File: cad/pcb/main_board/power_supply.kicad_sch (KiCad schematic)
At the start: 7 parts

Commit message: VDDA, BOOT SEL
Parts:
- removed C7: 100nF, symbol Device:C
- removed C8: 1uF, symbol Device:C
- added C10: 1uF, symbol Device:C
- added C11: 100nF, symbol Device:C
- added L1: L, symbol Device:L
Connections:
- net VSSA: now also C10.2, C11.2
- net VBAT renamed +3V3
- net +3V3: now also L1.1
- net VSS renamed GND
- new net VDDA: C10.1, C11.1, L1.2

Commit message: Thermo Couple Pins
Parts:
- C2: value 100nF -> 4u7F
- C6: value 4u7F -> 100nF
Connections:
- net VSSA is gone; now on net GND: C10.2, C11.2

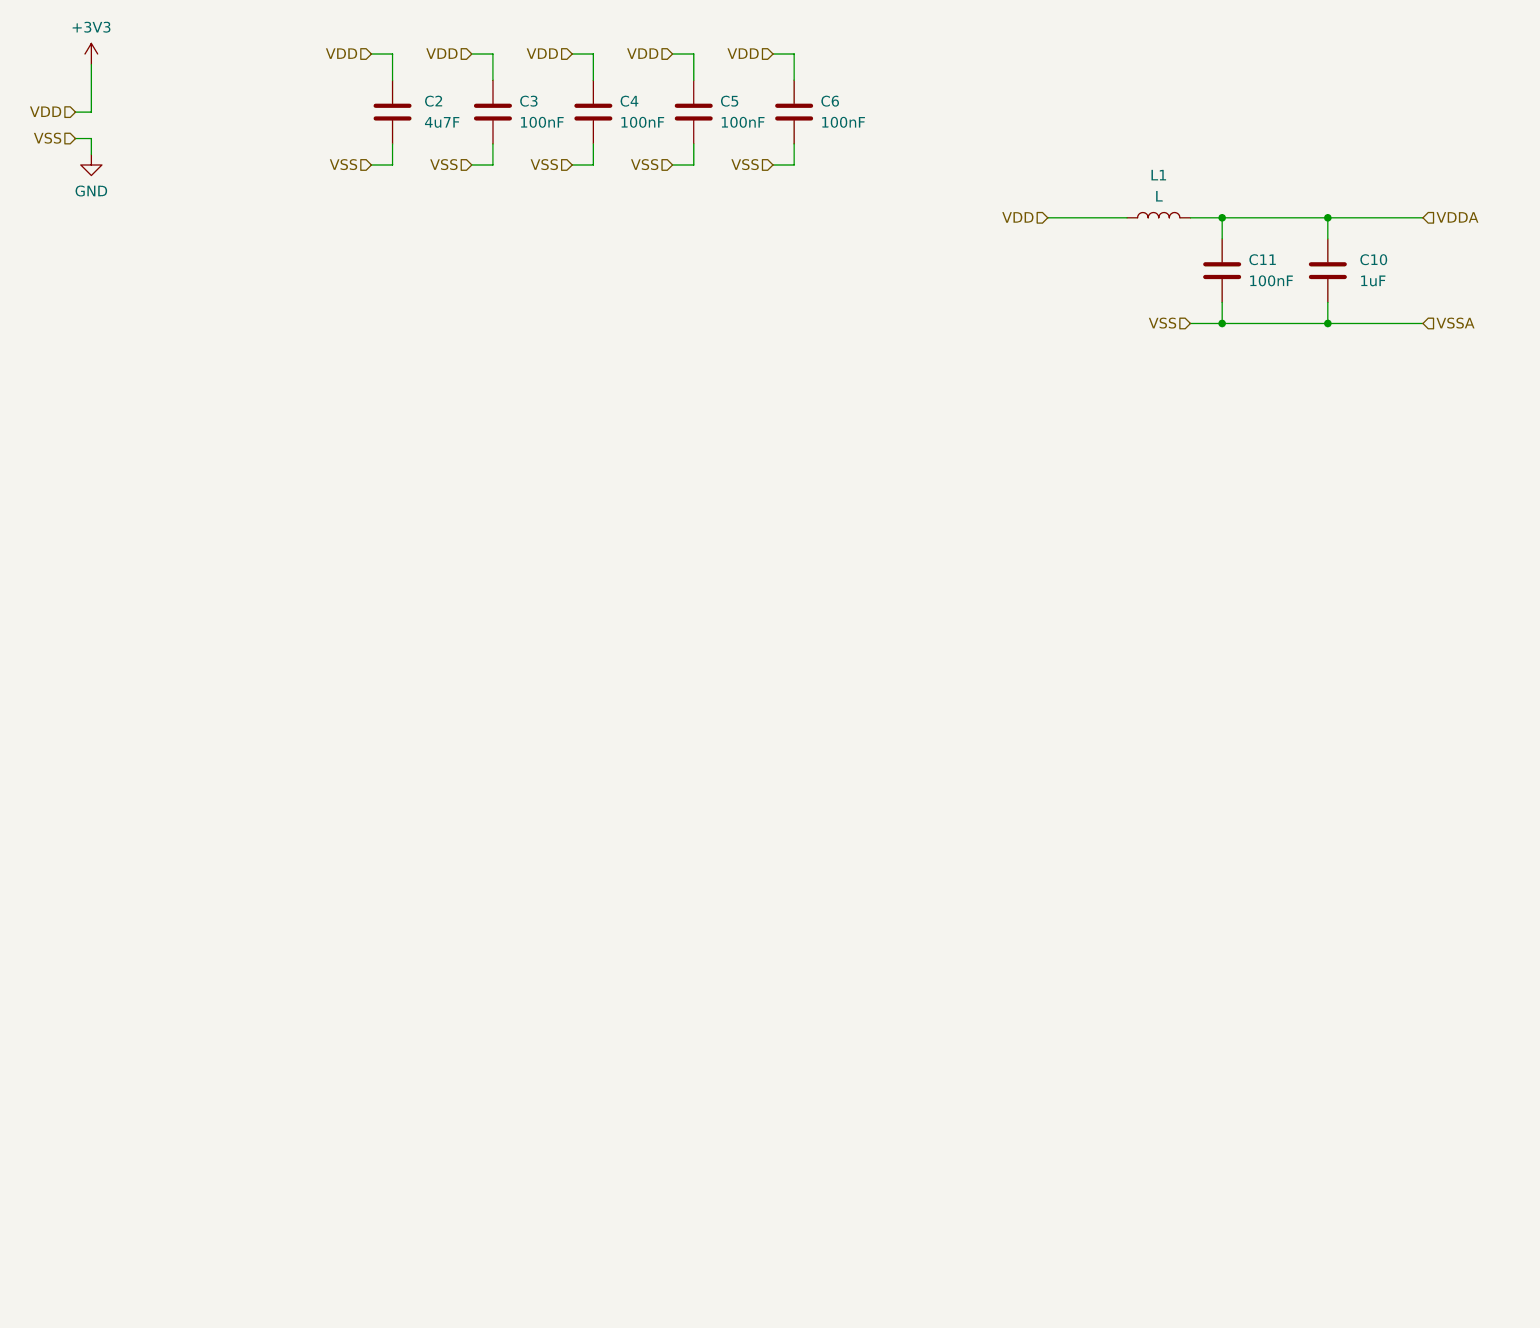
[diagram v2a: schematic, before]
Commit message: Adding Voltage Regulators, Adding SD Card Symbol
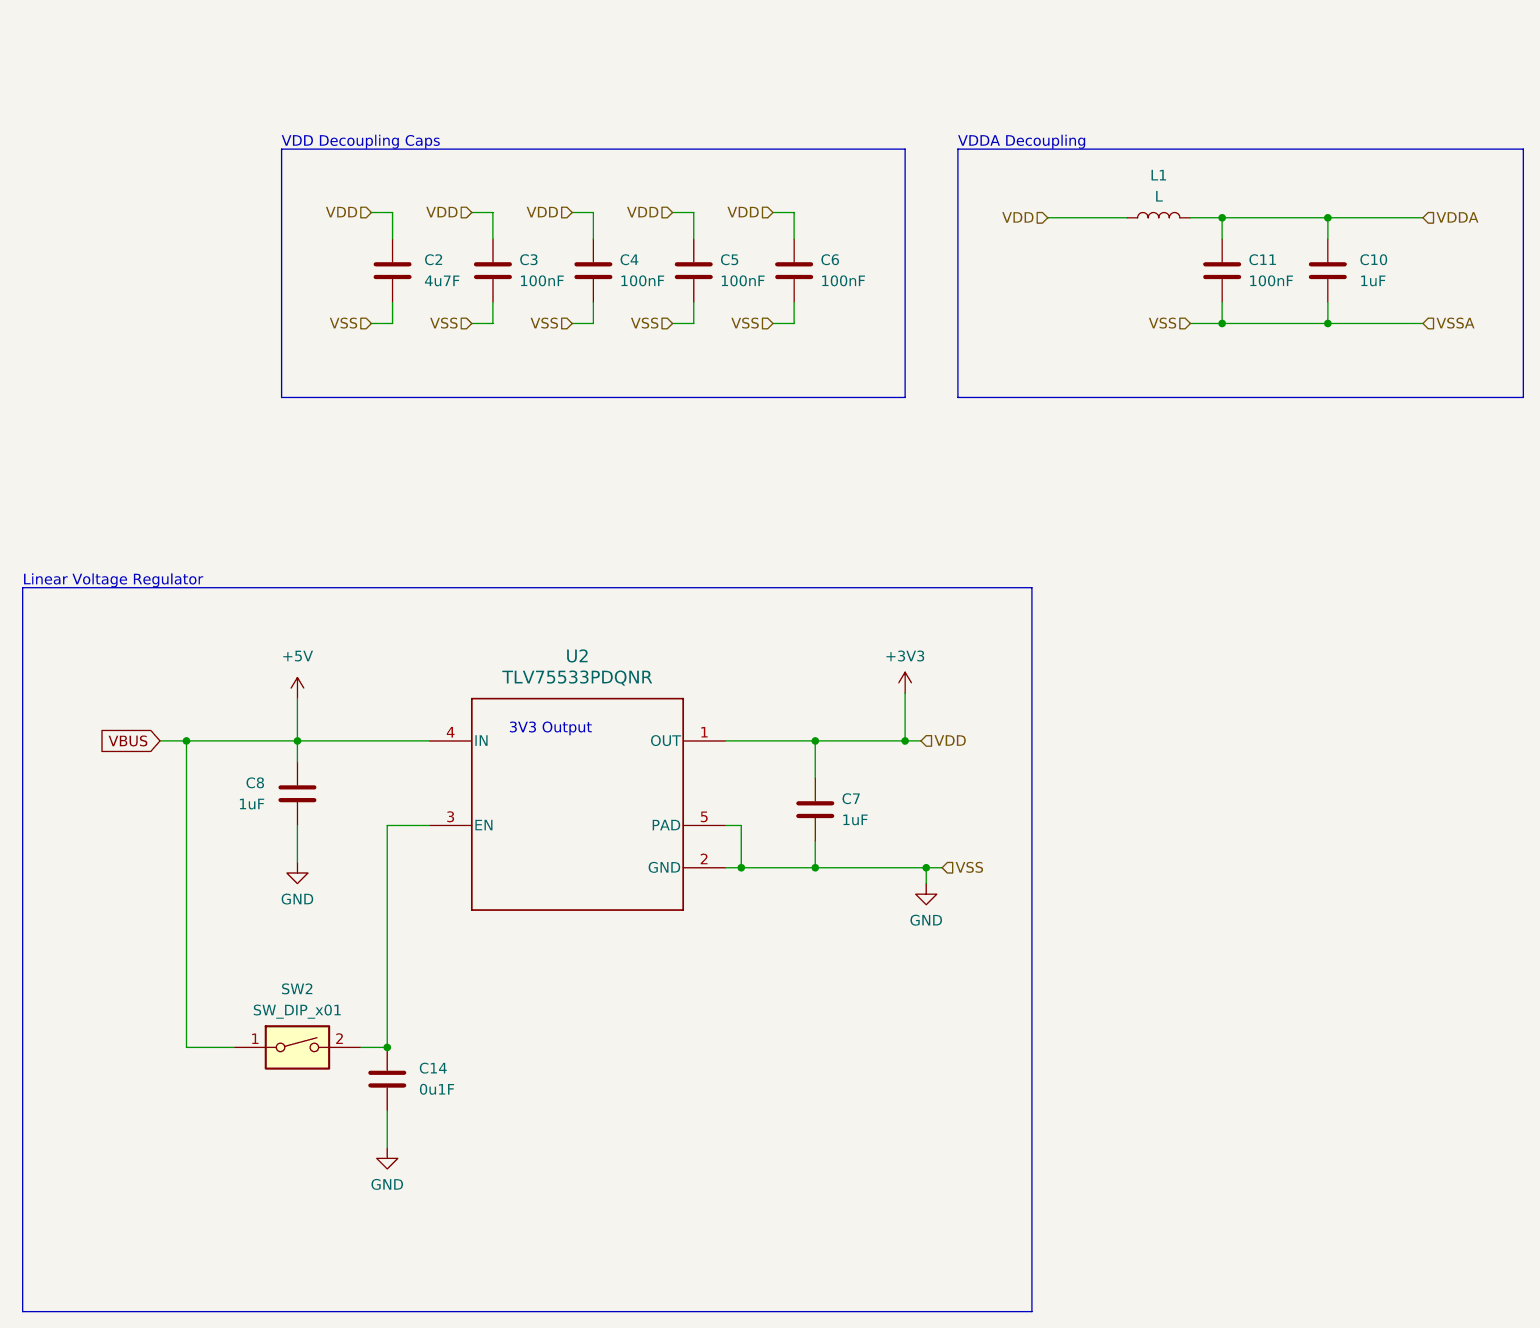
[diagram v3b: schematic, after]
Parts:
- added C14: 0u1F, symbol Device:C
- added C7, C8: 1uF, symbol Device:C
- added SW2: SW_DIP_x01, symbol Switch:SW_DIP_x01
- added U2: TLV75533PDQNR, DQN0004A, symbol local:TLV75533PDQNR
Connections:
- net +3V3: now also C7.1, U2.1 (OUT)
- net GND: now also C14.2, C7.2, C8.1, U2.2 (GND), U2.5 (PAD)
- new net: C14.1, SW2.2, U2.3 (EN)
- new net +5V: C8.2, SW2.1, U2.4 (IN)
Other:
- note added: "3V3 Output"
- note added: "Linear Voltage Regulator"
- note added: "VDD Decoupling Caps"
- note added: "VDDA Decoupling"
- moved on the sheet: C2, C3, C4, C5, C6

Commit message: Add Aisler files
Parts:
- C10, C11, C14, C2, C3, C4, C5, C6, C7, C8: footprint (none) -> Capacitor_SMD:C_0805_2012Metric
- L1: footprint (none) -> Inductor_SMD:L_0805_2012Metric
- SW2: footprint (none) -> Button_Switch_SMD:SW_DIP_SPSTx01_Slide_6.7x4.1mm_W6.73mm_P2.54mm_LowProfile_JPin
- U2: footprint DQN0004A -> local:DQN0004A
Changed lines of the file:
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@@
       (effects (font (size 1.27 1.27)) (justify left))
     )
-    (property "Footprint" "" (at 127.9652 69.85 0)
+    (property "Footprint" "Capacitor_SMD:C_0805_2012Metric" (at 127.9652 69.85 0)
       (effects (font (size 1.27 1.27)) hide)
     )
@@
       (effects (font (size 1.27 1.27)) (justify left))
     )
-    (property "Footprint" "" (at 115.9002 69.85 0)
+    (property "Footprint" "Capacitor_SMD:C_0805_2012Metric" (at 115.9002 69.85 0)
       (effects (font (size 1.27 1.27)) hide)
     )
@@
       (effects (font (size 1.27 1.27)) (justify right))
     )
-    (property "Footprint" "" (at 80.3402 125.095 0)
+    (property "Footprint" "Capacitor_SMD:C_0805_2012Metric" (at 80.3402 125.095 0)
       (effects (font (size 1.27 1.27)) hide)
     )
@@
       (effects (font (size 1.27 1.27)) (justify left))
     )
-    (property "Footprint" "" (at 191.4652 69.85 0)
+    (property "Footprint" "Capacitor_SMD:C_0805_2012Metric" (at 191.4652 69.85 0)
       (effects (font (size 1.27 1.27)) hide)
     )
@@
       (effects (font (size 1.27 1.27)) (justify left))
     )
-    (property "Footprint" "" (at 140.0302 69.85 0)
+    (property "Footprint" "Capacitor_SMD:C_0805_2012Metric" (at 140.0302 69.85 0)
       (effects (font (size 1.27 1.27)) hide)
     )
@@
       (effects (font (size 1.27 1.27)))
     )
-    (property "Footprint" "" (at 79.375 159.385 0)
+    (property "Footprint" "Button_Switch_SMD:SW_DIP_SPSTx01_Slide_6.7x4.1mm_W6.73mm_P2.54mm_LowProfile_JPin" (at 79.375 159.385 0)
       (effects (font (size 1.27 1.27)) hide)
     )
@@
       (effects (font (size 1.27 1.27)) (justify left))
     )
-    (property "Footprint" "" (at 204.1652 69.85 0)
+    (property "Footprint" "Capacitor_SMD:C_0805_2012Metric" (at 204.1652 69.85 0)
       (effects (font (size 1.27 1.27)) hide)
     )
@@
       (effects (font (size 1.524 1.524)))
     )
-    (property "Footprint" "DQN0004A" (at 113.03 130.175 0)
+    (property "Footprint" "local:DQN0004A" (at 113.03 130.175 0)
       (effects (font (size 1.27 1.27) italic) hide)
     )
@@
       (effects (font (size 1.27 1.27)) (justify left))
     )
-    (property "Footprint" "" (at 103.8352 69.85 0)
+    (property "Footprint" "Capacitor_SMD:C_0805_2012Metric" (at 103.8352 69.85 0)
       (effects (font (size 1.27 1.27)) hide)
     )
@@
       (effects (font (size 1.27 1.27)) (justify left))
     )
-    (property "Footprint" "" (at 142.5702 134.62 0)
+    (property "Footprint" "Capacitor_SMD:C_0805_2012Metric" (at 142.5702 134.62 0)
       (effects (font (size 1.27 1.27)) hide)
     )
@@
       (effects (font (size 1.27 1.27)))
     )
-    (property "Footprint" "" (at 182.88 59.69 0)
+    (property "Footprint" "Inductor_SMD:L_0805_2012Metric" (at 182.88 59.69 0)
       (effects (font (size 1.27 1.27)) hide)
     )
@@
       (effects (font (size 1.27 1.27)) (justify left))
     )
-    (property "Footprint" "" (at 91.1352 167.005 0)
+    (property "Footprint" "Capacitor_SMD:C_0805_2012Metric" (at 91.1352 167.005 0)
       (effects (font (size 1.27 1.27)) hide)
     )
@@
       (effects (font (size 1.27 1.27)) (justify left))
     )
-    (property "Footprint" "" (at 91.7702 69.85 0)
-      (effects (font (size 1.27 1.27)) hide)
-    )
+    (property "Footprint" "Capacitor_SMD:C_0805_2012Metric" (at 91.7702 69.85 0)
+      (effects (font (size 1.27 1.27)) hide)
+    )

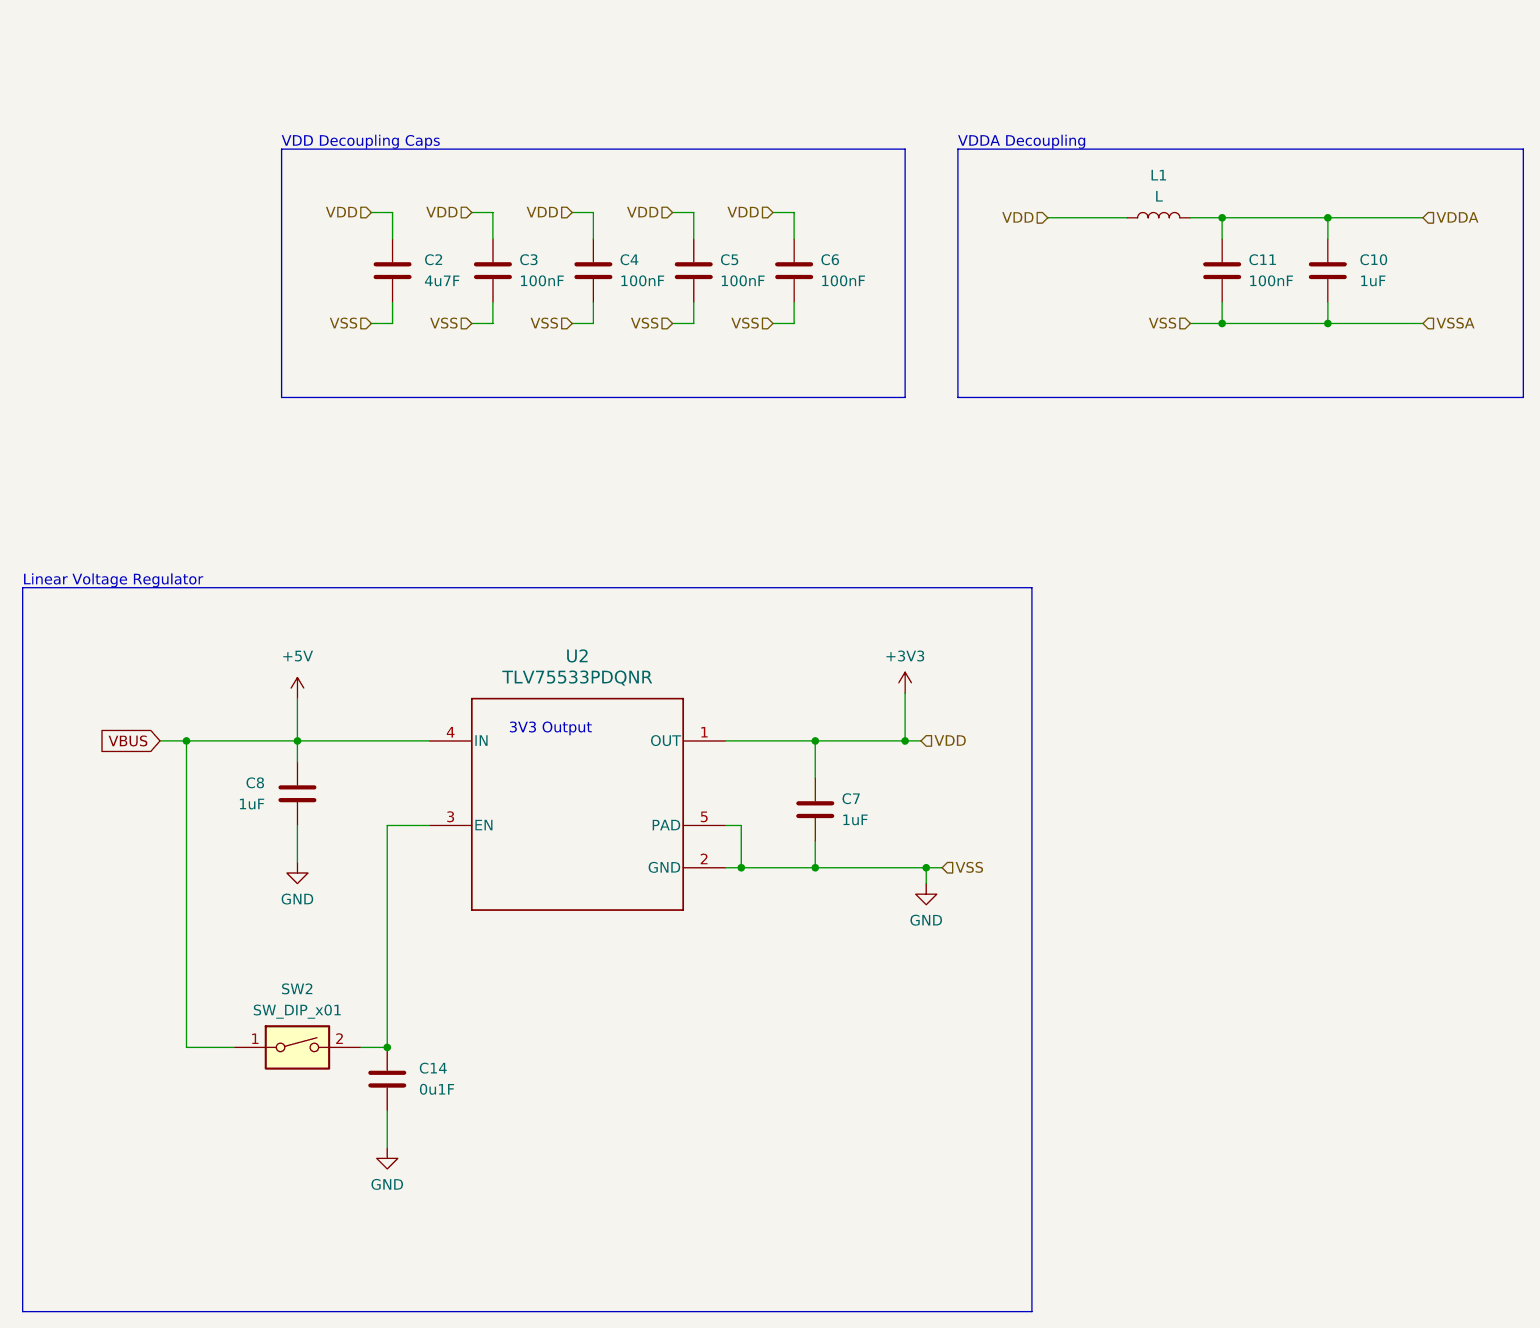
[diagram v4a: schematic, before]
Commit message: First Layout of Voltage Regulator, Status LED note, add pulldown resistor for Voltage Regulator Enable
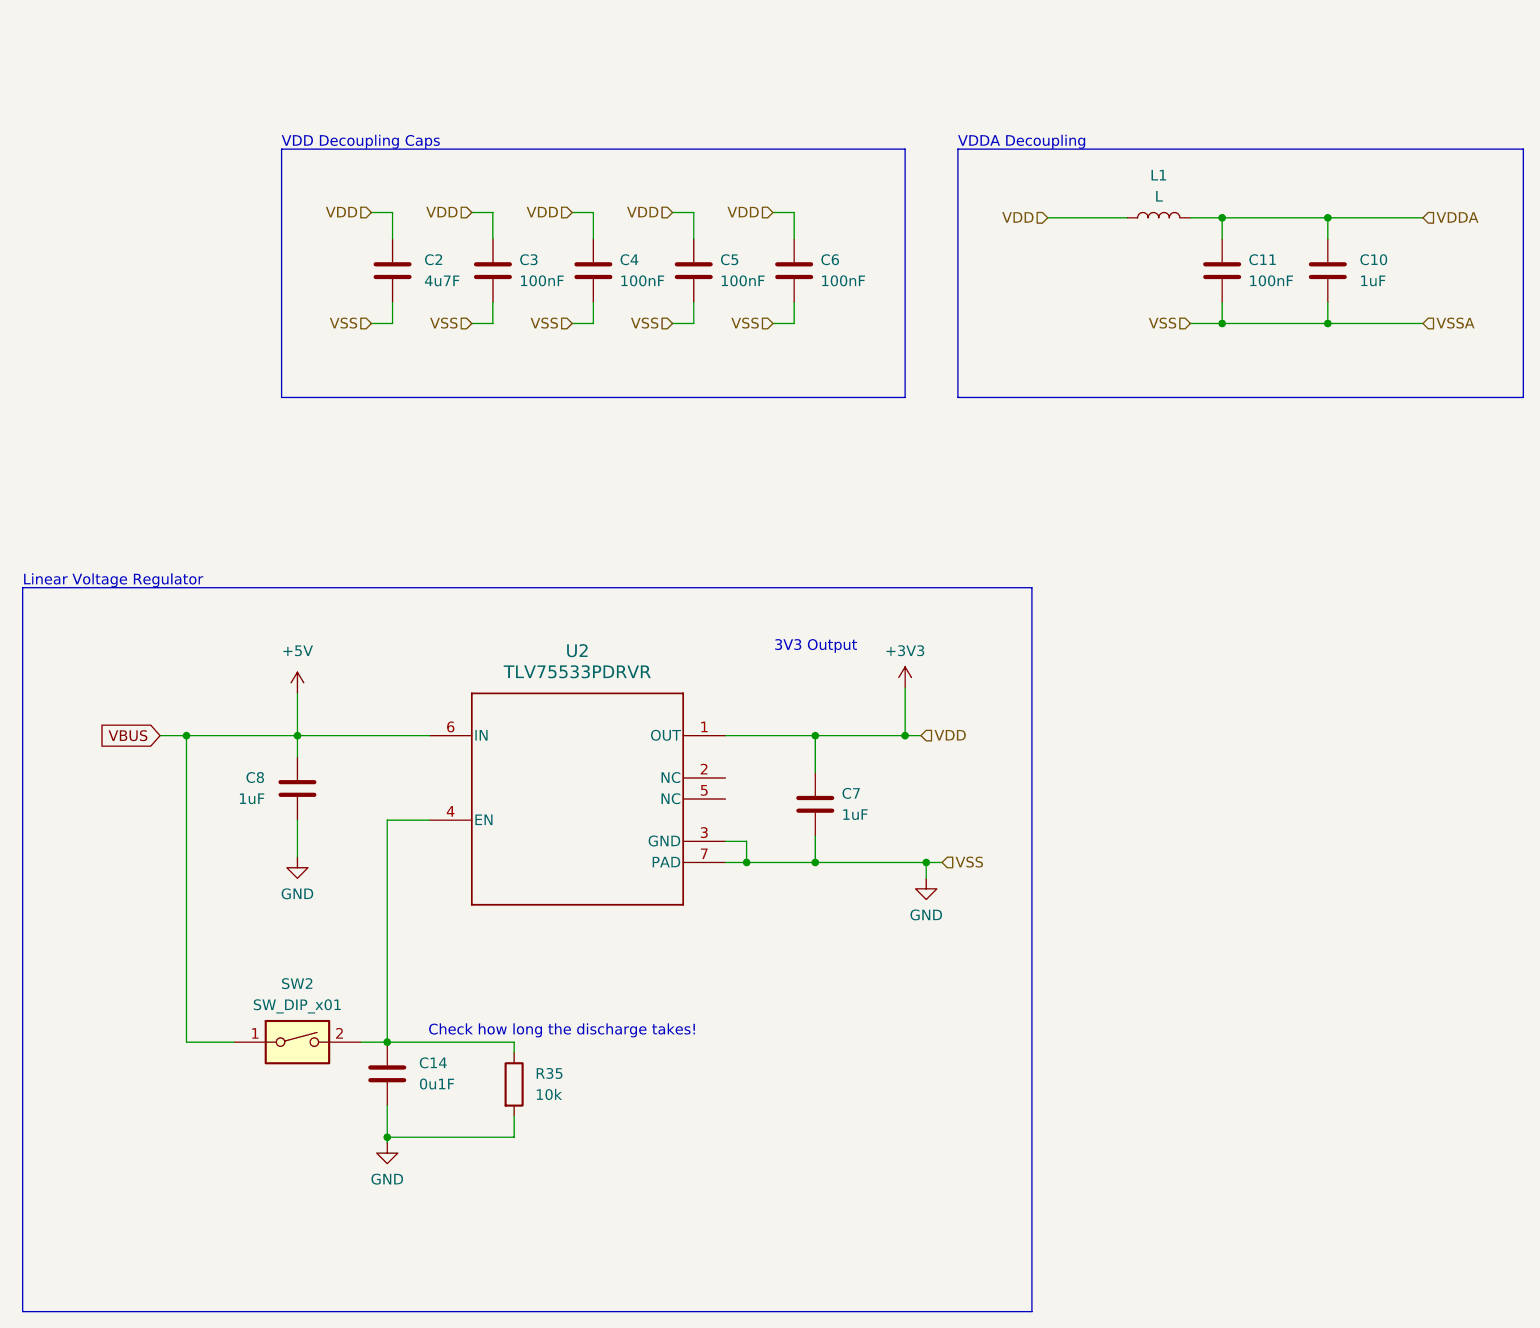
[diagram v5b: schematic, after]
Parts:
- removed U2: TLV75533PDQNR, local:DQN0004A, symbol local:TLV75533PDQNR
- added R35: 10k, Resistor_SMD:R_0805_2012Metric, symbol Device:R
- added U2: TLV75533PDRVR, local:DRV0006A, symbol local:TLV75533PDRVR
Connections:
- net +3V3: now also U2.1 (OUT)
- net +5V: now also U2.6 (IN)
- net GND: now also R35.2, U2.3 (GND), U2.7 (PAD)
- net at C14.1, SW2.2: now also R35.1, U2.4 (EN)
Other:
- note added: "Check how long the discharge takes!"
- moved on the sheet: C14, C7, C8, SW2
